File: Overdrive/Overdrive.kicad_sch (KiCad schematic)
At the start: 50 parts, among them J1 IN, J2 DC IN, J3 OUT, Q1 MMBT2222A, Q2 MMBT2222A, SW1 SW_SPDT, U1 TL072

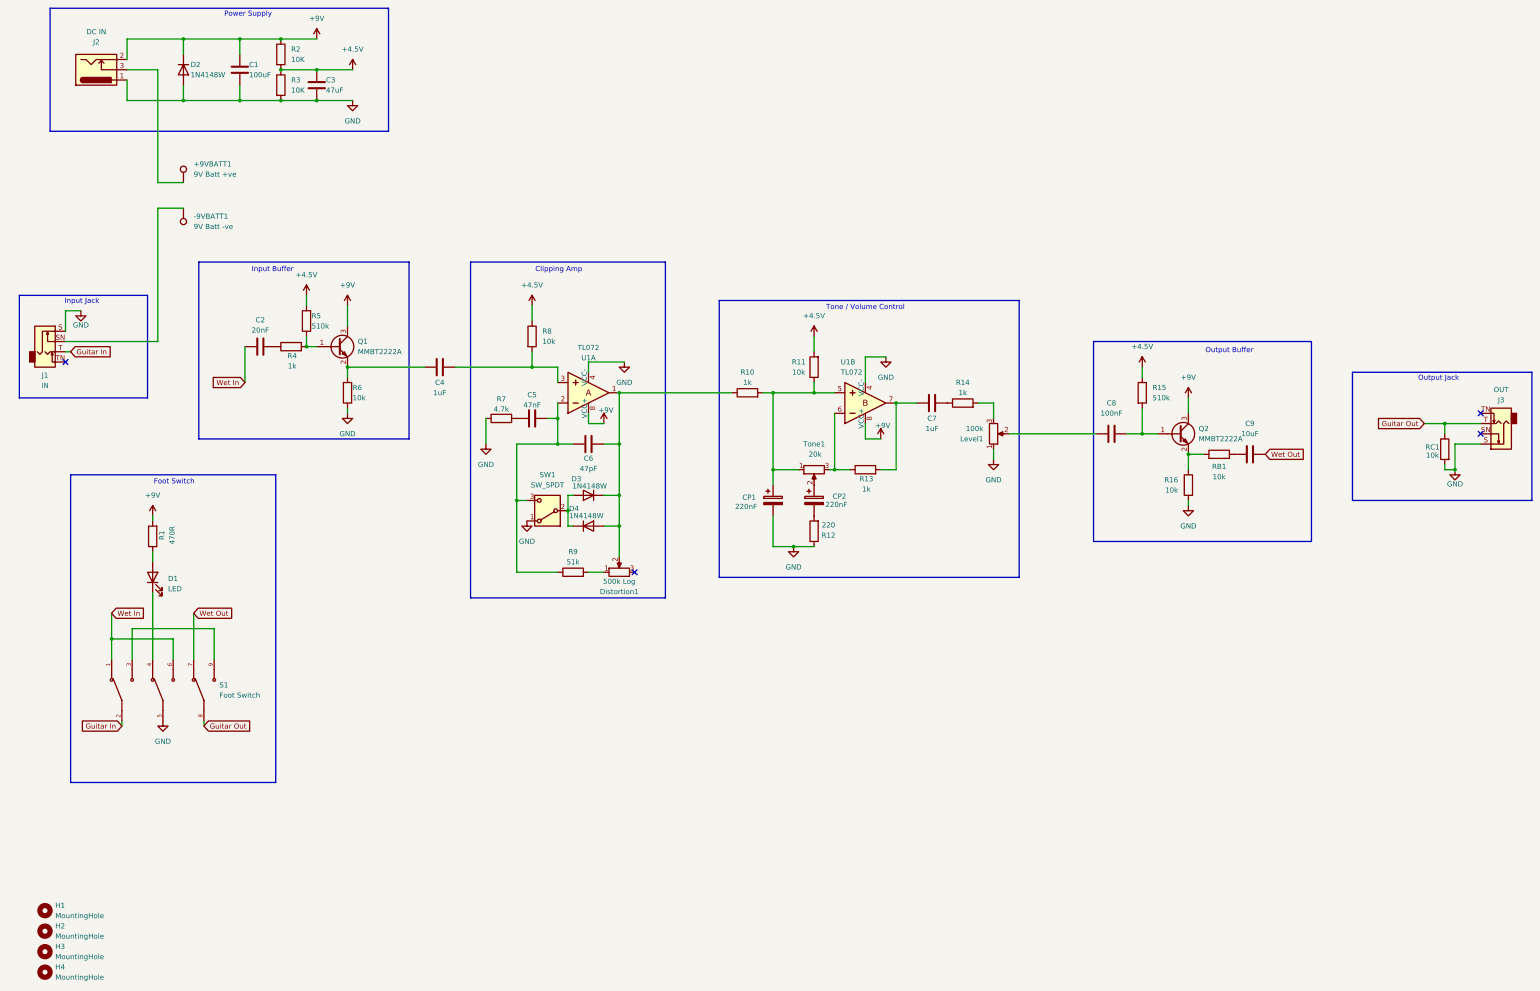
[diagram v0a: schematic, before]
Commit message: added FX loop into its own sheet
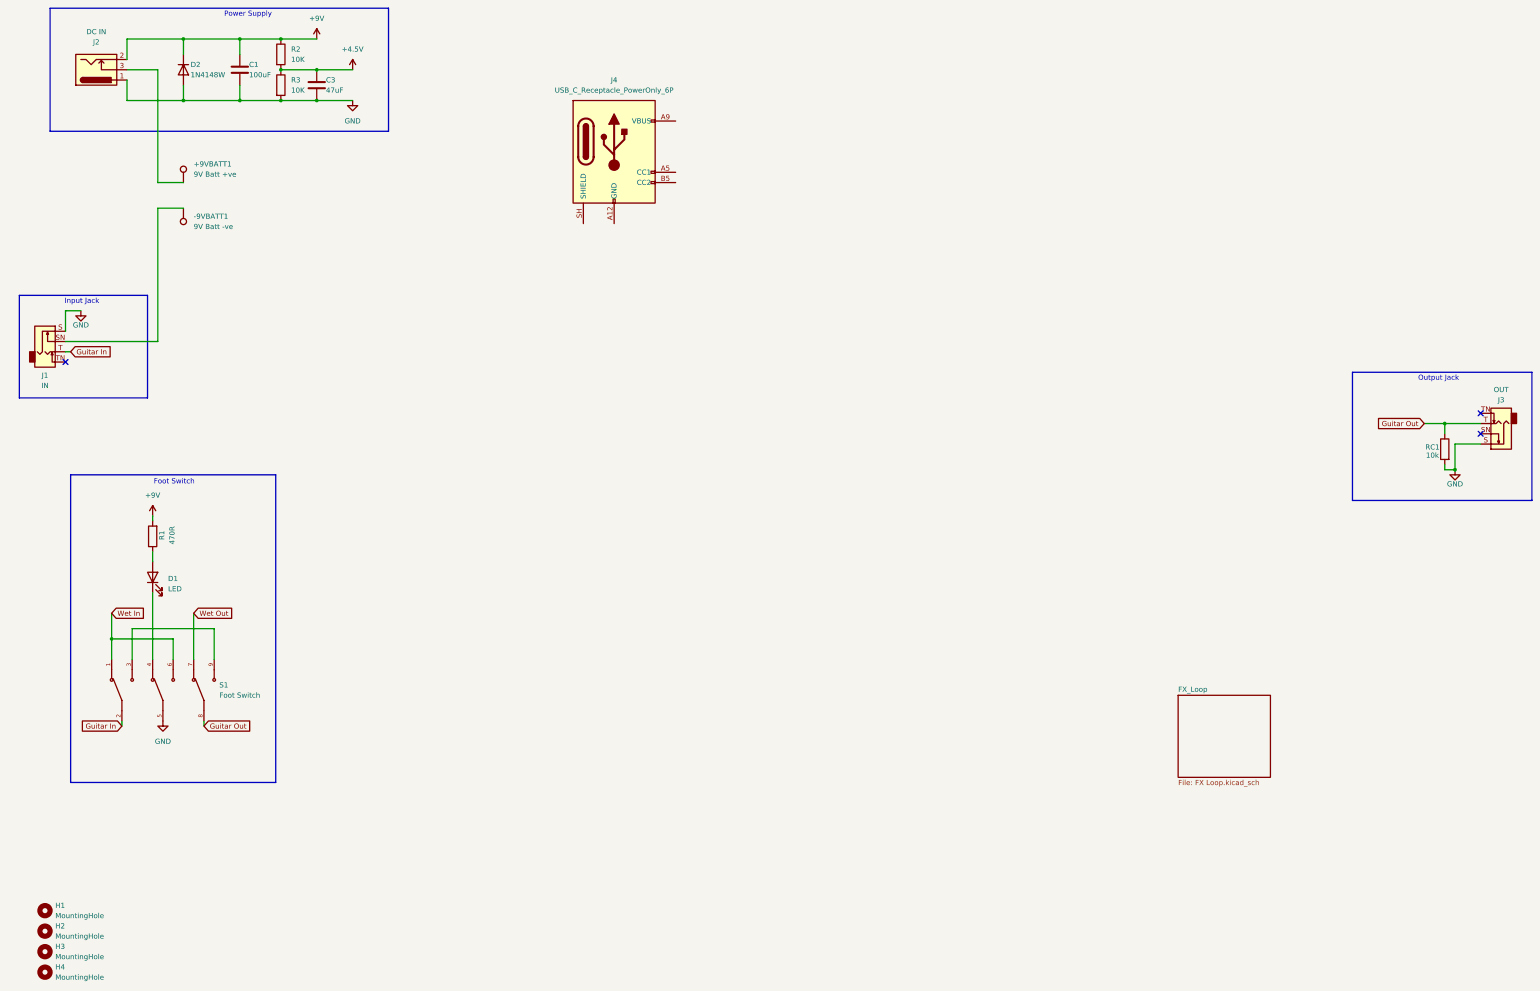
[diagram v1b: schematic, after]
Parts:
- removed C2: 20nF, Capacitor_SMD:C_0603_1608Metric, symbol Device:C
- removed C4, C7: 1uF, Capacitor_SMD:C_0603_1608Metric, symbol Device:C
- removed C5: 47nF, Capacitor_SMD:C_0603_1608Metric, symbol Device:C
- removed C6: 47pF, Capacitor_SMD:C_0603_1608Metric, symbol Device:C
- removed C8: 100nF, Capacitor_SMD:C_0603_1608Metric, symbol Device:C
- removed C9: 10uF, Capacitor_SMD:C_0603_1608Metric, symbol Device:C
- removed CP1, CP2: 220nF, Capacitor_THT:CP_Radial_D5.0mm_P2.50mm, symbol Device:C_Polarized
- removed D3, D4: 1N4148W, Diode_SMD:D_SOD-123, symbol Diode:1N4148W
- removed Distortion1: 500k Log, Potentiometer_THT:Potentiometer_RK097_Single_Vertical, symbol Device:R_Potentiometer
- removed Level1: 100k, Potentiometer_THT:Potentiometer_RK097_Single_Vertical, symbol Device:R_Potentiometer
- removed Q1, Q2: MMBT2222A, Package_TO_SOT_SMD:SOT-23, symbol Transistor_BJT:MMBT2222A
- removed R10, R13, R14, R4: 1k, Resistor_SMD:R_0603_1608Metric, symbol Device:R
- removed R11, R16, R6, R8, RB1: 10k, Resistor_SMD:R_0603_1608Metric, symbol Device:R
- removed R12: 220, Resistor_SMD:R_0603_1608Metric, symbol Device:R
- removed R15, R5: 510k, Resistor_SMD:R_0603_1608Metric, symbol Device:R
- removed R7: 4.7k, Resistor_SMD:R_0603_1608Metric, symbol Device:R
- removed R9: 51k, Resistor_SMD:R_0603_1608Metric, symbol Device:R
- removed SW1: SW_SPDT, Button_Switch_THT:spdt switch custom, symbol Switch:SW_SPDT
- removed Tone1: 20k, Potentiometer_THT:Potentiometer_RK097_Single_Vertical, symbol Device:R_Potentiometer
- removed U1: TL072, Package_SO:SOIC-8_3.9x4.9mm_P1.27mm, symbol dk_Linear-Amplifiers-Instrumentation-OP-Amps-Buffer-Amps:TL072CP
- added J4: USB_C_Receptacle_PowerOnly_6P, symbol Connector:USB_C_Receptacle_PowerOnly_6P
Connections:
- new net: J4.A12 (GND), J4.B12 (GND)
- new net: J4.A9 (VBUS), J4.B9 (VBUS)
- no-connect marks 4 -> 3
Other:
- added sheet FX_Loop (FX Loop.kicad_sch)
- note removed: "Clipping Amp"
- note removed: "Input Buffer"
- note removed: "Output Buffer"
- note removed: "Tone / Volume Control"

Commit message: done PCB layout
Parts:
- removed +9VBATT1: 9V Batt +ve, TestPoint:TestPoint_THTPad_2.5x2.5mm_Drill1.2mm, symbol Connector:TestPoint
- removed -9VBATT1: 9V Batt -ve, TestPoint:TestPoint_THTPad_2.5x2.5mm_Drill1.2mm, symbol Connector:TestPoint
- removed H1, H2, H3, H4: MountingHole, MountingHole:MountingHole_3.2mm_M3_Pad_Via, symbol Mechanical:MountingHole
- removed J1: IN, Connector_Audio:Jack_6.35mm_Neutrik_NMJ6HFD2_Horizontal, symbol Connector_Audio:AudioJack2_Switch
- removed J2: DC IN, Connector_BarrelJack:BarrelJack_GCT_DCJ200-10-A_Horizontal, symbol Connector:Barrel_Jack_Switch
- removed J3: OUT, Connector_Audio:Jack_6.35mm_Neutrik_NMJ6HFD2_Horizontal, symbol Connector_Audio:AudioJack2_Switch
- removed J4: USB_C_Receptacle_PowerOnly_6P, symbol Connector:USB_C_Receptacle_PowerOnly_6P
- removed RC1: 10k, Resistor_SMD:R_0603_1608Metric, symbol Device:R
- removed S1: Foot Switch, Button_Switch_THT:3PDT Foot Switch, symbol (3PDT) Footswitch:FS57003PLT2B2M2QE
- added C10: 10uF, Capacitor_SMD:C_0603_1608Metric, symbol Device:C
- added C2: 47uF, Capacitor_SMD:C_0603_1608Metric, symbol Device:C
- added C4: 47nF, Capacitor_SMD:C_0603_1608Metric, symbol Device:C
- added C5: 47pF, Capacitor_SMD:C_0603_1608Metric, symbol Device:C
- added C6, C7: 220nF, Capacitor_SMD:C_0603_1608Metric, symbol Device:C
- added C8: 1uF, Capacitor_SMD:C_0603_1608Metric, symbol Device:C
- added C9: 100nF, Capacitor_SMD:C_0603_1608Metric, symbol Device:C
- added D3: 1N4148W, Diode_SMD:D_SOD-123, symbol Diode:1N4148W
- added Distortion1: 500k Log, PTV09A-4020F-A504:POT_PTV09A-4020F_BRN, symbol Device:R_Potentiometer
- added J1: 303C-321018-30-04, 303C-321018-30-04:ATTEND_303C-321018-30-04, symbol 303C-321018-30-04:303C-321018-30-04
- added Level1: 100k, PTV09A-4020F-A504:POT_PTV09A-4020F_BRN, symbol Device:R_Potentiometer
- added Q1, Q2: MMBT2222A, Package_TO_SOT_SMD:SOT-23, symbol Transistor_BJT:MMBT2222A
- added R10, R13, R14: 1k, Resistor_SMD:R_0603_1608Metric, symbol Device:R
- added R11, R16, R6, R7, RB1: 10k, Resistor_SMD:R_0603_1608Metric, symbol Device:R
- added R12: 220R, Resistor_SMD:R_0603_1608Metric, symbol Device:R
- added R15: 510k, Resistor_SMD:R_0603_1608Metric, symbol Device:R
- added R4, R5: 10K, Resistor_SMD:R_0603_1608Metric, symbol Device:R
- added R8: 4.7k, Resistor_SMD:R_0603_1608Metric, symbol Device:R
- added R9: 51k, Resistor_SMD:R_0603_1608Metric, symbol Device:R
- added Tone1: 20k, PTV09A-4020F-A504:POT_PTV09A-4020F_BRN, symbol Device:R_Potentiometer
- added U1: TL072, Package_SO:SOIC-8_3.9x4.9mm_P1.27mm, symbol dk_Linear-Amplifiers-Instrumentation-OP-Amps-Buffer-Amps:TL072CP
- C1: value 100uF -> 20nF; footprint Capacitor_SMD:C_1206_3216Metric -> Capacitor_SMD:C_0603_1608Metric
- C3: value 47uF -> 1uF; footprint Capacitor_SMD:C_1206_3216Metric -> Capacitor_SMD:C_0603_1608Metric
- R1: value 470R -> 1k
- R2: value 10K -> 470R
- R3: value 10K -> 510k
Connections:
- net +4.5V: now also R3.2, C2.1, R11.2, R15.1, R4.2, R5.1, R7.1; no longer C3.1, R2.2, R3.1
- net +9V: now also J1.1, Q1.3 (C), Q2.3 (C), R4.1, U1.8 (VCC+), U1.8 (VCC+); no longer C1.1, D2.1 (K), R1.2
- net GND: now also D1.1 (K), C2.2, C6.1, J1.4, Level1.1, R12.1, R16.2, R5.2, R6.1, R8.1, U1.4 (VCC-), U1.4 (VCC-); no longer C1.2, C3.2, D2.2 (A), R3.2
- net at R1.1: now also C1.2; no longer D1.2 (A)
- new net: C6.2, R10.2, R11.1, Tone1.1, U1.5
- new net: C7.1, Tone1.2
- new net: R13.1, Tone1.3, U1.6
- new net: C5.2, D2.1 (K), D3.2 (A), Distortion1.2, R10.1, U1.1
- new net: C4.2, C5.1, D2.2 (A), D3.1 (K), R9.2, U1.2
- new net: C8.1, R13.2, U1.7
- new net: C8.2, R14.1
- new net: Distortion1.1, R9.1
- new net: Q2.2 (E), R16.1, RB1.2
- new net: C7.2, R12.2
- new net: C10.1, RB1.1
- new net: Q1.1 (B), R1.2, R3.1
- new net: C3.1, Q1.2 (E), R6.2
- new net: C9.2, Q2.1 (B), R15.2
- new net: Level1.3, R14.2
- new net: C9.1, Level1.2
- new net: C3.2, R7.2, U1.3
- new net: C4.1, R8.2
- new net: D1.2 (A), R2.2
- new net FX_IN: C1.1, J1.3
- new net FX_OUT: C10.2, J1.2
- no-connect marks 3 -> 1
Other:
- removed sheet FX_Loop
- note added: "Clipping Amp"
- note added: "Input Buffer"
- note added: "Input Connector"
- note added: "Output Buffer"
- note added: "Tone / Volume Control"
- note added: "Voltage Divider"
- note removed: "Foot Switch"
- note removed: "Input Jack"
- note removed: "Output Jack"
- note removed: "Power Supply"
